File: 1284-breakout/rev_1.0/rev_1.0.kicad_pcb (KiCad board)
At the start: 2 copper layers, 71 parts, among them J1 ICSP, J10 RR_rh, J11 Tach, J12 MAX31865, J13 Micro_SD_Card_Det_Hirose_DM3AT, J14 Ulti_GPS_v3, J2 RF_BHE, J3 Output_BHE, J4 IMU_bout, J5 LF_BHE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

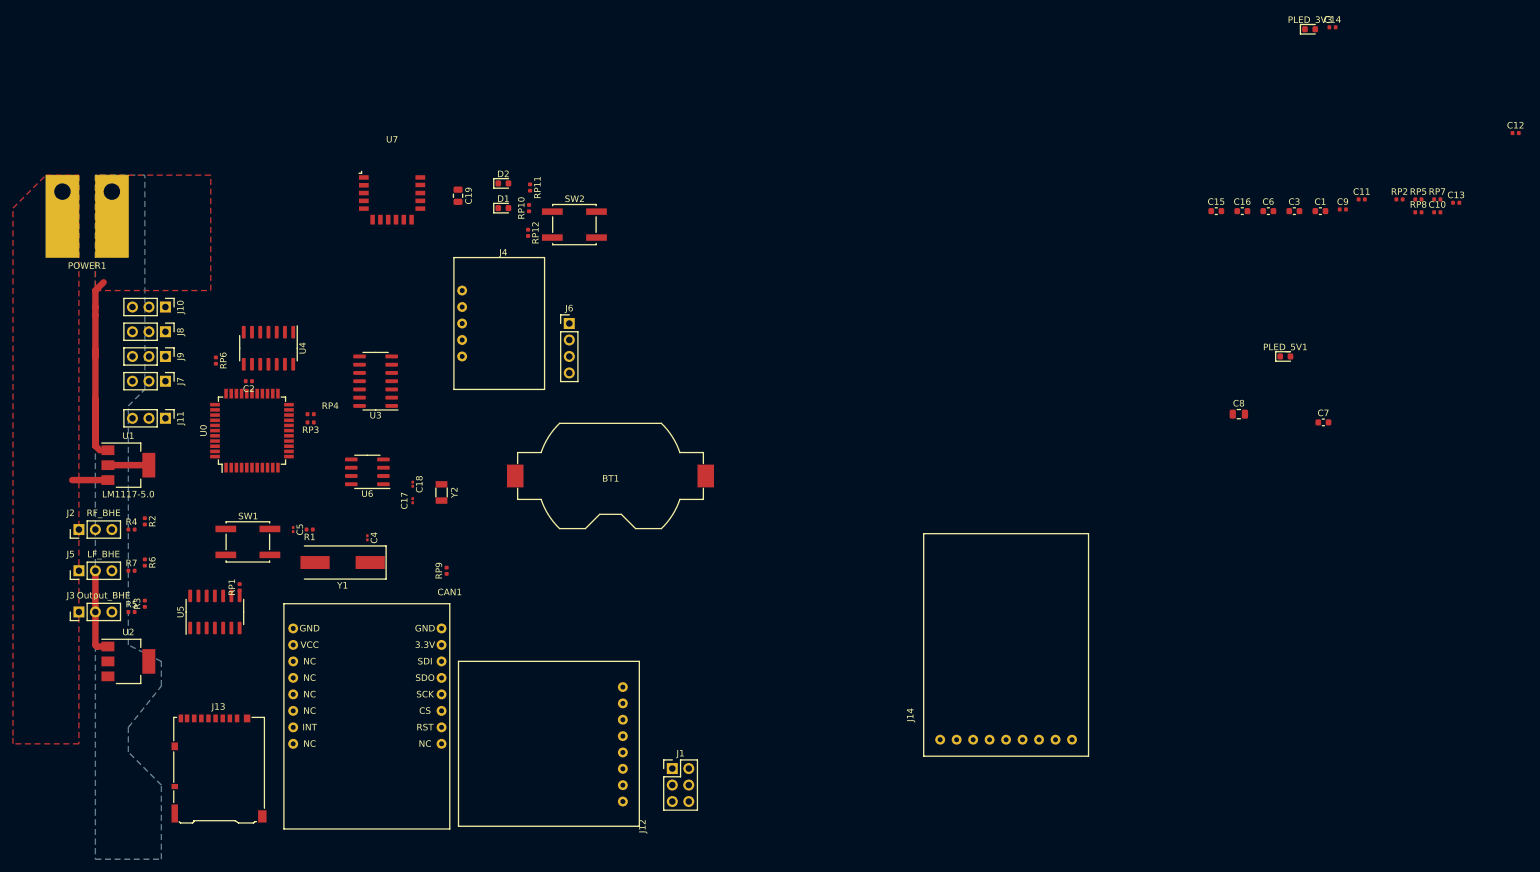
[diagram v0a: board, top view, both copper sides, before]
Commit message: added stitching vias
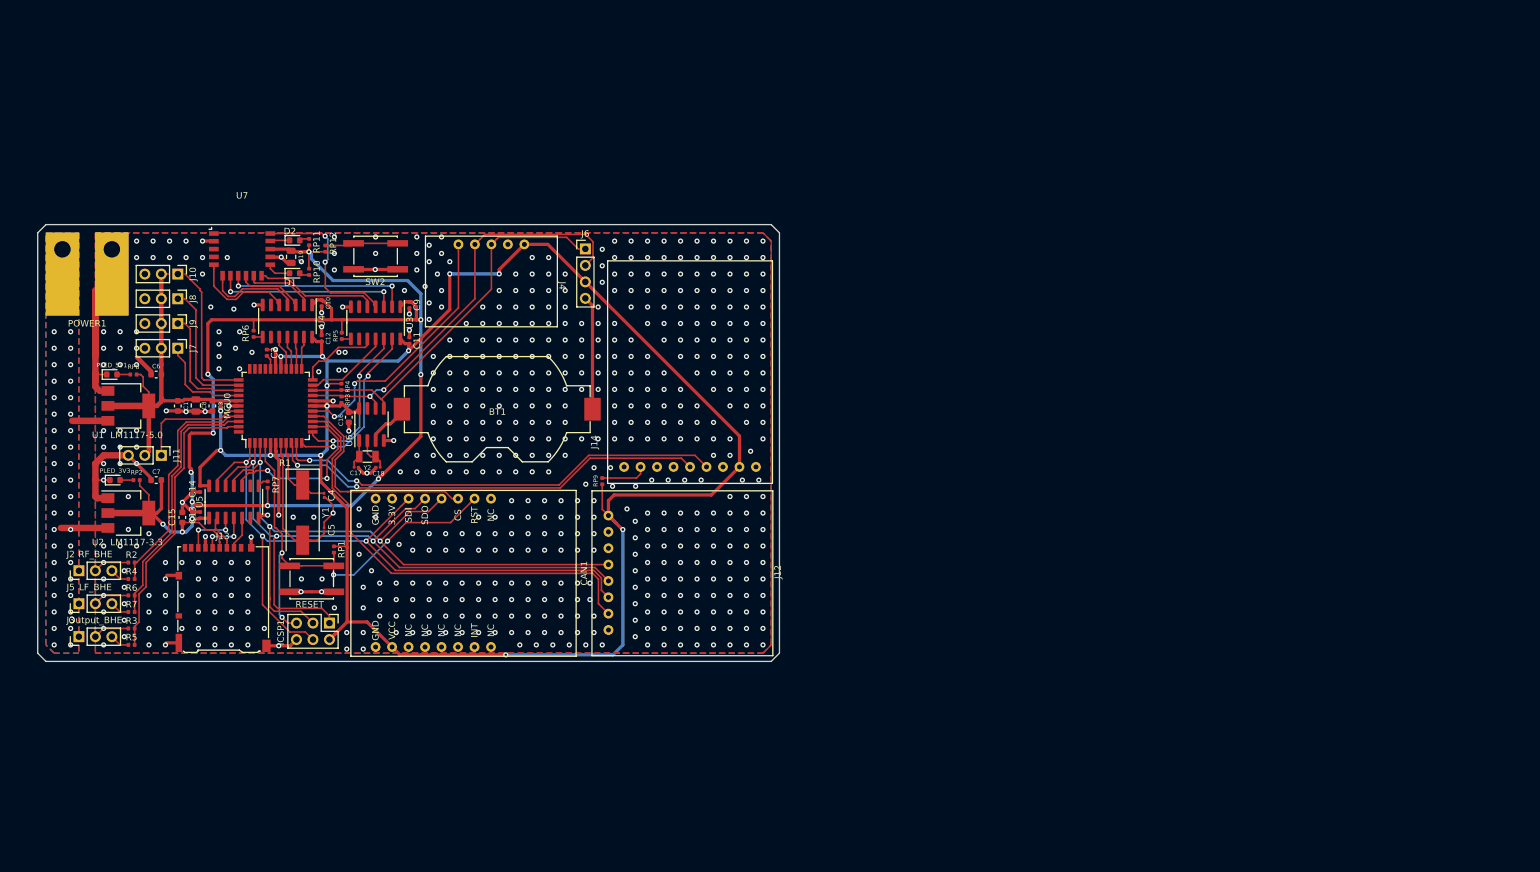
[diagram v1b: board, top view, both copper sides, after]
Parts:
- moved RP8 199.6 mm to (-146.5, 65.0)
- moved C13 199.5 mm to (-136.3, 86.7), turned to 90 degrees
- moved RP2 199.4 mm to (-146.1, 81.3)
- moved PLED_3V3 196.8 mm to (-149.4, 81.3)
- moved C14 188.4 mm to (-136.3, 82.6), turned to 90 degrees
- moved C12 186.7 mm to (-117.5, 59.5), turned to -90 degrees
- moved RP7 185.5 mm to (-125.9, 82.0), turned to 90 degrees
- moved PLED_5V1 180.8 mm to (-149.9, 65.0)
- moved C7 180.1 mm to (-143.0, 81.3), turned to 180 degrees
- moved C1 178.6 mm to (-139.7, 69.8), turned to -90 degrees
- moved C6 173.2 mm to (-143.0, 65.0), turned to 180 degrees
- moved C10 172.5 mm to (-117.5, 54.0), turned to -90 degrees
- moved C3 169.4 mm to (-134.4, 69.8), turned to -90 degrees
- moved RP5 167.2 mm to (-114.4, 59.1), turned to -90 degrees
- moved C15 166.2 mm to (-139.0, 87.0), turned to 90 degrees
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- renumbered J1 to ICSP1, U0 to MCU0, SW1 to RESET
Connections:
- J4 pad 5: /PCINT23 -> /PCINT31
- U1 pad 4: (no net) -> +5V
- U2 pad 4: (no net) -> +3V3
- U3 pad 4: /P0_0 -> /P2_0
- U3 pad 5: /P3_6 -> /P0_0
- U4 pad 10: /PCINT22 -> /PCINT23
- U4 pad 11: /PCINT21 -> /PCINT22
- U4 pad 12: /PCINT20 -> /PCINT21
- U4 pad 13: /PCINT28 -> /PCINT20
- U4 pad 3: /P2_0 -> /P3_6
- U5 pad 10: /PCINT31 -> /PCINT28
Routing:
- net +5V: track 6.30 -> 354.4 mm, vias 0 -> 13
- net +3V3: track 0.00 -> 219.6 mm, vias 0 -> 12
- net GND: track 50.9 -> 178.3 mm, vias 0 -> 605
- net /MOSI: track 0.00 -> 110.3 mm, vias 0 -> 3
- net /MISO: track 0.00 -> 108.7 mm, vias 0 -> 3
- net /SCK: track 0.00 -> 106.7 mm, vias 0 -> 3
- net /RESET: track 0.00 -> 70.2 mm, vias 0 -> 4
- net /TX0: track 0.00 -> 69.9 mm, vias 0 -> 2
- net /PCINT29: track 0.00 -> 68.8 mm
- net /RX0: track 0.00 -> 68.3 mm, vias 0 -> 2
- net /SCL: track 0.00 -> 65.3 mm, vias 0 -> 2
- net /SDA: track 0.00 -> 59.3 mm
- net /PCINT11: track 0.00 -> 44.6 mm
- net /PCINT31: track 0.00 -> 41.0 mm, vias 0 -> 2
- net /PCINT10: track 0.00 -> 40.3 mm
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- added copper zone on B.Cu, net +7.5V
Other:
- board outline added: 114.3 x 67.3 mm
